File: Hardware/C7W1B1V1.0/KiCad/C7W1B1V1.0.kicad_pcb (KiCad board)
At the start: 2 copper layers, 20 x 20 mm, 0 parts

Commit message: początkowy schemat
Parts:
- added C1: 100n/16V/X5R, Capacitor_SMD:C_0402_1005Metric, F.Cu at (156.0, 74.0)
- added C10: 100n/16V/X5R, Capacitor_SMD:C_0402_1005Metric, F.Cu at (191.6, 52.9)
- added C11: 10u/6.3V/X5R, Capacitor_SMD:C_0402_1005Metric, F.Cu at (189.0, 69.0)
- added C12: 10u/6.3V/X5R, Capacitor_SMD:C_0402_1005Metric, F.Cu at (189.3, 73.0)
- added C13: 510p/10V/C0G, Capacitor_SMD:C_0402_1005Metric, F.Cu at (185.1, 75.7)
- added C14: 10u/6.3V/X5R, Capacitor_SMD:C_0402_1005Metric, F.Cu at (191.9, 69.0)
- added C15: 10u/6.3V/X5R, Capacitor_SMD:C_0402_1005Metric, F.Cu at (189.0, 71.0)
- added C16: 10u/6.3V/X5R, Capacitor_SMD:C_0402_1005Metric, F.Cu at (182.2, 77.7)
- added C17: 10u/6.3V/X5R, Capacitor_SMD:C_0402_1005Metric, F.Cu at (186.5, 73.0)
- added C18: 100n/16V/X5R, Capacitor_SMD:C_0402_1005Metric, F.Cu at (182.2, 75.7)
- added C19: 100n/16V/X5R, Capacitor_SMD:C_0402_1005Metric, F.Cu at (183.0, 86.0)
- added C2: 100n/16V/X5R, Capacitor_SMD:C_0402_1005Metric, F.Cu at (159.7, 69.2)
- added C20: 10u/6.3V/X5R, Capacitor_SMD:C_0402_1005Metric, F.Cu at (176.0, 92.5)
- added C21: 10u/6.3V/X5R, Capacitor_SMD:C_0402_1005Metric, F.Cu at (174.8, 97.0)
- added C22: 10u/6.3V/X5R, Capacitor_SMD:C_0402_1005Metric, F.Cu at (176.0, 90.5)
- added C23: 100n/16V/X5R, Capacitor_SMD:C_0402_1005Metric, F.Cu at (174.8, 95.0)
- added C3: 100n/16V/X5R, Capacitor_SMD:C_0402_1005Metric, F.Cu at (158.9, 72.0)
- added C4: 100n/16V/X5R, Capacitor_SMD:C_0402_1005Metric, F.Cu at (151.6, 76.4)
- added C5: 8p/16V/C0G, Capacitor_SMD:C_0402_1005Metric, F.Cu at (154.5, 76.4)
- added C6: 8p/16V/C0G, Capacitor_SMD:C_0402_1005Metric, F.Cu at (162.5, 69.2)
- added C7: 100n/16V/X5R, Capacitor_SMD:C_0402_1005Metric, F.Cu at (158.8, 52.9)
- added C8: 100n/16V/X5R, Capacitor_SMD:C_0402_1005Metric, F.Cu at (185.4, 61.0)
- added C9: 100n/16V/X5R, Capacitor_SMD:C_0402_1005Metric, F.Cu at (182.5, 63.0)
- added D1: PMEG4010CEGWX, Diode_SMD:D_SOD-123, F.Cu at (176.5, 69.7)
- added D2: BZX384B3V3-E3-08, Diode_SMD:D_SOD-323, F.Cu at (175.7, 77.0)
- added F1: 0686F2000-01, Fuse:Fuse_0603_1608Metric, F.Cu at (176.6, 86.3)
- added IC1: USBLC6-2P6, Footprints:USBLC62P6, F.Cu at (150.8, 97.9)
- added IC2: LMR62421XSD_NOPB, Footprints:SON95P300X300X80-7N, F.Cu at (182.0, 70.4)
- added IC3: S-8261AAXMD-G2XT2U, Footprints:SOT95P275X135-6N, F.Cu at (165.6, 96.4)
- added J1: Waveshare 12955, Connector_PinHeader_2.54mm:PinHeader_2x04_P2.54mm_Vertical, F.Cu at (149.6, 54.2)
- added J2: PMS3003, Connector_PinHeader_2.54mm:PinHeader_2x04_P2.54mm_Vertical, F.Cu at (176.2, 54.2)
- added J3: USB4105GFA120, Footprints:GCT_USB4105GFA120, F.Cu at (154.1, 91.7)
- added J4: Conn_01x02_Male, TerminalBlock:TerminalBlock_bornier-2_P5.08mm, F.Cu at (166.2, 89.5)
- added L1: CBC3225T470MR, Inductor_SMD:L_1210_3225Metric, F.Cu at (176.4, 73.5)
- added Q1: PMDPB30XNAX, Footprints:PMDPB30XNAX, F.Cu at (170.8, 96.6)
- added R1: 10k/5%/0.063W, Resistor_SMD:R_0402_1005Metric, F.Cu at (156.0, 72.0)
- added R10: 30k/1%/0.063W, Resistor_SMD:R_0402_1005Metric, F.Cu at (179.3, 76.6)
- added R11: 10k/1%/0.063W, Resistor_SMD:R_0402_1005Metric, F.Cu at (183.6, 73.7)
- added R12: 10k/1%/0.063W, Resistor_SMD:R_0402_1005Metric, F.Cu at (186.1, 71.0)
- added R13: 10k/1%/0.063W, Resistor_SMD:R_0402_1005Metric, F.Cu at (180.7, 73.7)
- added R14: 10k/5%/0.063W, Resistor_SMD:R_0402_1005Metric, F.Cu at (154.6, 100.5)
- added R15: 10k/5%/0.063W, Resistor_SMD:R_0402_1005Metric, F.Cu at (159.8, 96.1)
- added R16: 10k/5%/0.063W, Resistor_SMD:R_0402_1005Metric, F.Cu at (159.8, 99.7)
- added R17: 2k2/5%/0.063W, Resistor_SMD:R_0402_1005Metric, F.Cu at (162.7, 100.2)
- added R18: 2k2/5%/0.063W, Resistor_SMD:R_0402_1005Metric, F.Cu at (165.6, 99.7)
- added R19: 470/5%/0.063W, Resistor_SMD:R_0402_1005Metric, F.Cu at (176.0, 88.5)
- added R2: 10k/5%/0.063W, Resistor_SMD:R_0402_1005Metric, F.Cu at (148.7, 76.4)
- added R20: 100k/1%/0.063W, Resistor_SMD:R_0402_1005Metric, F.Cu at (159.0, 105.0)
- added R21: 100k/1%/0.063W, Resistor_SMD:R_0402_1005Metric, F.Cu at (161.9, 105.0)
- added R3: 10k/5%/0.063W, Resistor_SMD:R_0402_1005Metric, F.Cu at (155.9, 52.9)
- added R4: 10k/5%/0.063W, Resistor_SMD:R_0402_1005Metric, F.Cu at (182.6, 59.0)
- added R5: 10k/5%/0.063W, Resistor_SMD:R_0402_1005Metric, F.Cu at (188.7, 52.9)
- added R6: 10k/5%/0.063W, Resistor_SMD:R_0402_1005Metric, F.Cu at (182.6, 61.0)
- added R7: 10k/5%/0.063W, Resistor_SMD:R_0402_1005Metric, F.Cu at (185.5, 59.0)
- added R8: 10k/5%/0.063W, Resistor_SMD:R_0402_1005Metric, F.Cu at (188.7, 54.9)
- added R9: 10k/5%/0.063W, Resistor_SMD:R_0402_1005Metric, F.Cu at (186.1, 69.0)
- added U1: STM32L083CZTx, Package_QFP:LQFP-48_7x7mm_P0.5mm, F.Cu at (126.0, 71.0)
- added U2: BME688, Footprints:BME688, F.Cu at (184.2, 54.9)
- added U3: STC4054GR, Footprints:SOT95P280X110-5N, F.Cu at (155.8, 97.3)
- added Y1: 830106545501, Crystal:Crystal_SMD_2012-2Pin_2.0x1.2mm, F.Cu at (156.4, 69.6)

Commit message: Dodano projekt Cube
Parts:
- added C24: 100n/16V/X5R, Capacitor_SMD:C_0402_1005Metric, F.Cu at (86.6, 112.9)
- added C25: 100n/16V/X5R, Capacitor_SMD:C_0402_1005Metric, F.Cu at (83.7, 116.0)
- added C7: 100n/16V/X5R, Capacitor_SMD:C_0402_1005Metric, F.Cu at (-69.3, 121.4)
- added R22: 470/5%/0.063W, Resistor_SMD:R_0402_1005Metric, F.Cu at (92.7, 103.3)
- added R23: 100k/1%/0.063W, Resistor_SMD:R_0402_1005Metric, F.Cu at (83.5, 110.0)
- added R24: 100k/1%/0.063W, Resistor_SMD:R_0402_1005Metric, F.Cu at (89.8, 103.9)
- added U4: W25N512GVEIG, Footprints:SON127P800X600X80-9N-D, F.Cu at (-75.8, 142.7)
- added U5: STC4054GR, Footprints:SOT95P280X110-5N, F.Cu at (81.4, 104.7)
- C1, C2: value 100n/16V/X5R -> 8p/16V/C0G
- C11, C12: value 10u/6.3V/X5R -> 100n/16V/X5R
- C13: value 510p/10V/C0G -> 10u/6.3V/X5R
- C18: value 100n/16V/X5R -> 510p/10V/C0G
- C19, C23: value 100n/16V/X5R -> 10u/6.3V/X5R
- C21: value 10u/6.3V/X5R -> 10n/16V/X5R
- C5, C6: value 8p/16V/C0G -> 100n/16V/X5R
- J1: value Waveshare 12955 -> PMS3003
- J2: value PMS3003 -> USB4105GFA120; footprint Connector_PinHeader_2.54mm:PinHeader_2x04_P2.54mm_Vertical -> Footprints:GCT_USB4105GFA120
- J3: value USB4105GFA120 -> Conn_01x02_Male; footprint Footprints:GCT_USB4105GFA120 -> TerminalBlock:TerminalBlock_bornier-2_P5.08mm
- J4: value Conn_01x02_Male -> Waveshare 12955; footprint TerminalBlock:TerminalBlock_bornier-2_P5.08mm -> Connector_PinHeader_2.54mm:PinHeader_2x04_P2.54mm_Vertical
- R10: value 30k/1%/0.063W -> 10k/5%/0.063W
- R11, R12, R13: value 10k/1%/0.063W -> 10k/5%/0.063W
- R16: value 10k/5%/0.063W -> 2k2/5%/0.063W
- R17: value 2k2/5%/0.063W -> 30k/1%/0.063W
- R18: value 2k2/5%/0.063W -> 10k/1%/0.063W
- R19: value 470/5%/0.063W -> 2k2/5%/0.063W
- R20, R21: value 100k/1%/0.063W -> 10k/1%/0.063W
- U3: value STC4054GR -> MB85RS512TPNF-G-JNERE1; footprint Footprints:SOT95P280X110-5N -> Footprints:SOIC127P600X175-8N
- moved R8 281.2 mm to (-80.2, 137.2), turned to 270 degrees
- moved R5 271.9 mm to (-75.8, 116.0)
- moved C11 269.7 mm to (-73.0, 132.8)
- moved C12 268.7 mm to (-71.2, 138.8)
- moved R10 268.5 mm to (-80.9, 142.8), turned to 270 degrees
- moved C10 266.7 mm to (-63.6, 130.4), turned to 180 degrees
- moved R9 266.0 mm to (-71.6, 135.1), turned to 270 degrees
- moved U2 263.4 mm to (-72.8, 113.0), turned to 270 degrees
- moved C8 263.3 mm to (-73.3, 109.5), turned to 90 degrees
- moved R11 263.1 mm to (-70.6, 141.5), turned to 270 degrees
- moved R6 262.2 mm to (-73.8, 116.0)
- moved R7 261.0 mm to (-65.5, 130.4), turned to 180 degrees
- moved R4 260.7 mm to (-71.8, 116.0), turned to 180 degrees
- moved C26 259.7 mm to (-82.1, 149.9), turned to 270 degrees
- moved C9 258.7 mm to (-71.9, 109.9), turned to 180 degrees
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- renumbered C7 to C26
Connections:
- C1 pad 1: +3V3 -> GND
- C1 pad 2: GND -> Net-(C1-Pad2)
- C11 pad 1: +BATT -> +3V3
- C12 pad 1: +BATT -> +3V3
- C13 pad 1: +5V -> /Power/USB_VBUS
- C13 pad 2: Net-(C13-Pad2) -> GND
- C14 pad 1: +5V -> VBUS
- C14 pad 2: Net-(C14-Pad2) -> GND
- C15 pad 1: +5V -> +BATT
- C15 pad 2: Net-(C14-Pad2) -> GND
- C16 pad 1: +5V -> +BATT
- C16 pad 2: Net-(C14-Pad2) -> GND
- C17 pad 1: +5V -> VBUS
- C17 pad 2: Net-(C14-Pad2) -> GND
- C18 pad 2: Net-(C14-Pad2) -> Net-(C18-Pad2)
- C19 pad 1: +3V3 -> +5V
- C19 pad 2: GND -> Net-(C19-Pad2)
- C2 pad 1: +3V3 -> GND
- C2 pad 2: GND -> Net-(C2-Pad2)
- C20 pad 1: VBUS -> +5V
- C20 pad 2: GND -> Net-(C19-Pad2)
- C21 pad 1: VBUS -> 5V_TEST
- C22 pad 1: VBUS -> +5V
- C22 pad 2: GND -> Net-(C19-Pad2)
- C23 pad 1: +BATT -> +5V
- C23 pad 2: GND1 -> Net-(C19-Pad2)
- C5 pad 1: GND -> +3V3
- C5 pad 2: Net-(C5-Pad2) -> GND
- C6 pad 1: GND -> +3V3
- C6 pad 2: Net-(C6-Pad2) -> GND
- F1 pad 2: VBUS -> /Power/USB_VBUS
- IC2 pad 4: Net-(C13-Pad2) -> Net-(C18-Pad2)
- J1 pad 1: +3V3 -> +5V
- J1 pad 2: E_INC_BUSY -> PMS_SET
- J1 pad 3: E_INC_RST -> GND
- J1 pad 4: E_INC_DC -> PMS_RST
- J1 pad 5: GND -> Net-(J1-Pad5)
- J1 pad 6: SCK -> PMS_RX
- J1 pad 7: MOSI -> Net-(J1-Pad7)
- J1 pad 8: E_INC_CS -> PMS_TX
- J4 pad 1: GND1 -> +3V3
- J4 pad 2: +BATT -> GND
- R1 pad 1: +3V3 -> Net-(R1-Pad1)
- R1 pad 2: Net-(R1-Pad2) -> GND
- R10 pad 1: +5V -> +3V3
- R10 pad 2: Net-(C13-Pad2) -> Net-(R10-Pad2)
- R11 pad 1: Net-(C13-Pad2) -> +3V3
- R11 pad 2: GND -> Net-(R11-Pad2)
- R12 pad 1: +5V -> GND
- R12 pad 2: 5V_TEST -> Net-(J2-PadA5)
- R13 pad 1: 5V_TEST -> GND
- R13 pad 2: GND -> Net-(J2-PadB5)
- R14 pad 1: GND -> 5V_EN
- R14 pad 2: Net-(J3-PadA5) -> GND
- R15 pad 1: GND -> +3V3
- R15 pad 2: Net-(J3-PadB5) -> ~CHRG_STATUS
- R16 pad 1: +3V3 -> Net-(R16-Pad1)
- R16 pad 2: ~CHRG_STATUS -> GND
- R17 pad 1: Net-(R17-Pad1) -> +5V
- R17 pad 2: GND -> Net-(C18-Pad2)
- R18 pad 1: Net-(IC3-Pad2) -> Net-(C18-Pad2)
- R19 pad 1: Net-(IC3-Pad5) -> Net-(IC3-Pad2)
- R19 pad 2: +BATT -> GND
- R2 pad 1: Net-(R2-Pad1) -> +3V3
- R2 pad 2: GND -> Net-(R2-Pad2)
- R20 pad 1: +BATT -> +5V
- R20 pad 2: BATT -> 5V_TEST
- R21 pad 1: BATT -> 5V_TEST
- R3 pad 2: Net-(R3-Pad2) -> GND
- R4 pad 1: Net-(R4-Pad1) -> +3V3
- R4 pad 2: GND -> Net-(R4-Pad2)
- R5 pad 2: Net-(R5-Pad2) -> SDA
- R6 pad 2: SDA -> SCL
- R7 pad 1: +3V3 -> +5V
- R7 pad 2: SCL -> PMS_SET
- R8 pad 1: +5V -> +3V3
- R8 pad 2: Net-(J2-Pad2) -> Net-(R8-Pad2)
- R9 pad 1: 5V_EN -> +3V3
- R9 pad 2: GND -> Net-(R9-Pad2)
- U1 pad 13: Net-(U1-Pad13) -> ~FLASH_CS
- U1 pad 14: Net-(U1-Pad14) -> ~FRAM_CS
- U1 pad 17: Net-(U1-Pad17) -> MISO
- U1 pad 2: Net-(U1-Pad2) -> ~CHRG_STATUS
- U1 pad 21: Net-(U1-Pad21) -> E_INC_DC
- U1 pad 28: Net-(U1-Pad28) -> PMS_SET
- U1 pad 29: Net-(U1-Pad29) -> PMS_RST
- U1 pad 3: Net-(C5-Pad2) -> Net-(C1-Pad2)
- U1 pad 30: Net-(U1-Pad30) -> PMS_RX
- U1 pad 31: Net-(U1-Pad31) -> PMS_TX
- U1 pad 39: E_INC_DC -> Net-(U1-Pad39)
- U1 pad 4: Net-(C6-Pad2) -> Net-(C2-Pad2)
- U1 pad 44: Net-(R2-Pad1) -> Net-(R1-Pad1)
- U1 pad 7: Net-(R1-Pad2) -> Net-(R2-Pad2)
- U2 pad 2: Net-(R5-Pad2) -> Net-(R4-Pad2)
- U2 pad 5: Net-(R4-Pad1) -> Net-(R3-Pad1)
- U3 pad 1: ~CHRG_STATUS -> ~FRAM_CS
- U3 pad 2: GND -> MISO
- U3 pad 3: +BATT -> Net-(R8-Pad2)
- U3 pad 4: VBUS -> GND
- U3 pad 5: Net-(R17-Pad1) -> MOSI
- Y1 pad 1: Net-(C5-Pad2) -> Net-(C1-Pad2)
- Y1 pad 2: Net-(C6-Pad2) -> Net-(C2-Pad2)
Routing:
- net E_INC_DC: track 0.00 -> 40.8 mm
- net E_INC_CS: track 0.00 -> 32.9 mm
- net E_INC_BUSY: track 0.00 -> 32.7 mm
- net SCK: track 0.00 -> 28.8 mm
- net E_INC_RST: track 0.00 -> 28.7 mm
- net MOSI: track 0.00 -> 23.9 mm, vias 0 -> 2
- net MISO: track 0.00 -> 21.9 mm, vias 0 -> 2
- net ~FLASH_CS: track 0.00 -> 16.7 mm
- net +3V3: track 0.00 -> 14.2 mm, vias 0 -> 3
- net SDA: track 0.00 -> 8.64 mm
- net Net-(IC1-Pad3): track 0.00 -> 8.53 mm
- net Net-(IC1-Pad1): track 0.00 -> 7.60 mm
- net PMS_TX: track 0.00 -> 6.68 mm
- net ~FRAM_CS: track 0.00 -> 6.53 mm
- net /Power/USB_VBUS: track 0.00 -> 6.47 mm
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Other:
- board outline removed
- copper layers 2 -> 4
- net class Default: clearance 0.2 -> 0.16; trace_width 0.25 -> 0.16
- rule trace_clearance: 0.2 -> 0.16
- rule trace_min: 0.2 -> 0.16

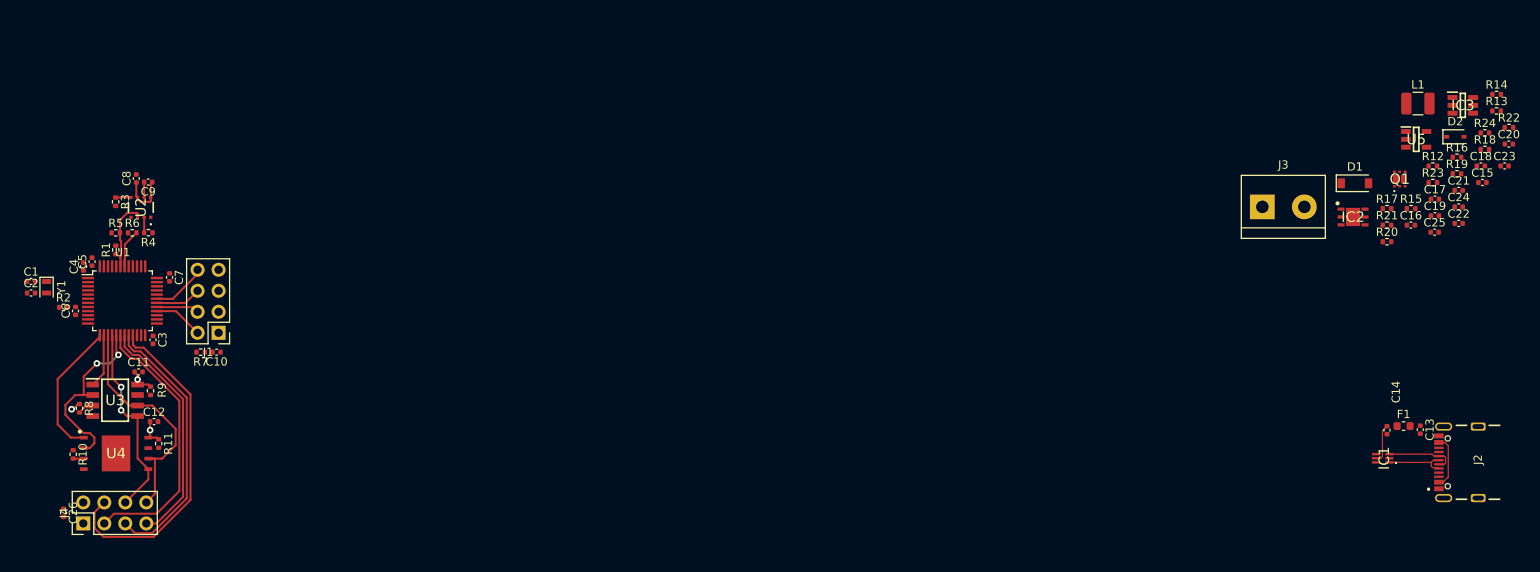
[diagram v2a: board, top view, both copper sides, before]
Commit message: Ukończono PCB. dodano pliki produkcyjne
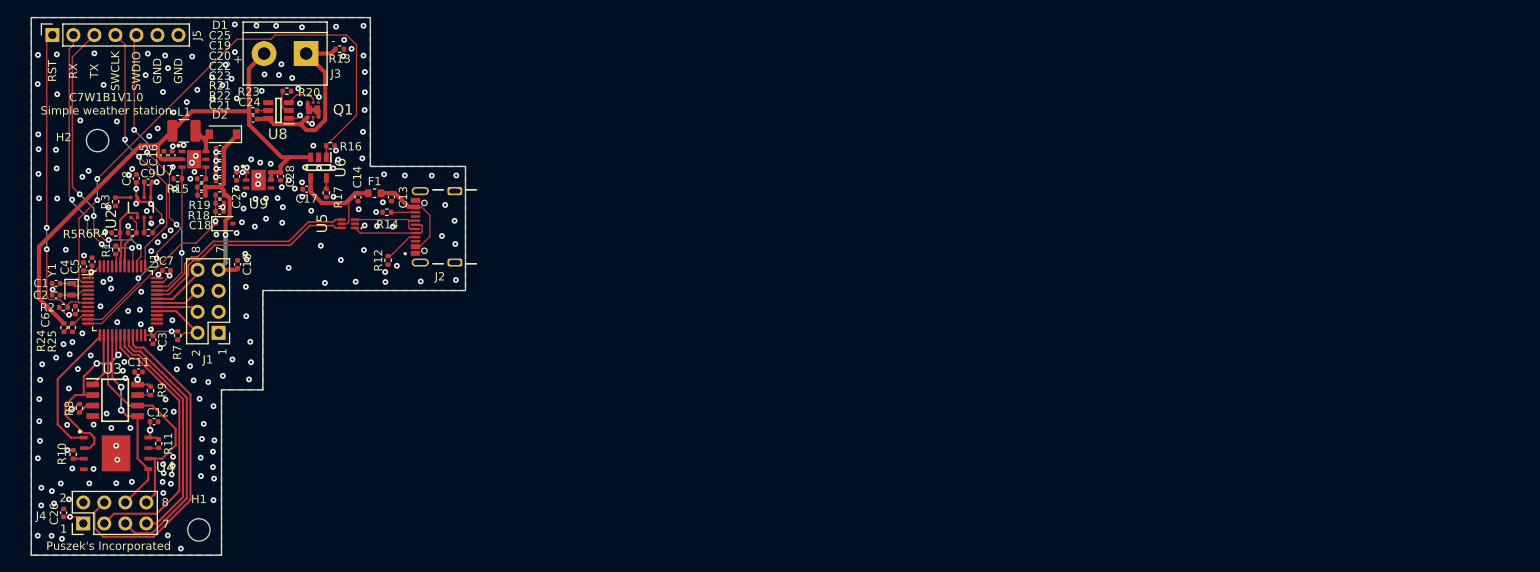
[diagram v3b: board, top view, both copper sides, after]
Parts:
- removed IC1: USBLC6-2P6, Footprints:USBLC62P6
- removed IC2: LMR62421XSD_NOPB, Footprints:SON95P300X300X80-7N
- removed IC3: S-8261AAXMD-G2XT2U, Footprints:SOT95P275X135-6N
- added C27: 10u/6.3V/X5R, Capacitor_SMD:C_0402_1005Metric, F.Cu at (-61.2, 109.2)
- added C28: 10u/6.3V/X5R, Capacitor_SMD:C_0402_1005Metric, F.Cu at (-55.9, 109.2)
- added H1: MountingHole, MountingHole:MountingHole_2.7mm_M2.5, F.Cu at (-65.7, 151.9)
- added H2: MountingHole, MountingHole:MountingHole_2.7mm_M2.5, F.Cu at (-78.0, 104.9)
- added J5: Conn_01x07, Connector_PinSocket_2.54mm:PinSocket_1x07_P2.54mm_Vertical, F.Cu at (-83.5, 92.1)
- added R25: 100k/1%/0.063W, Resistor_SMD:R_0402_1005Metric, F.Cu at (-81.0, 127.5)
- added U6: STC4054GR, Footprints:SOT95P280X110-5N, F.Cu at (-51.3, 108.1)
- added U7: LMR62421XSD_NOPB, Footprints:SON95P300X300X80-7N, F.Cu at (-66.3, 107.1)
- added U8: S-8261AAXMD-G2XT2U, Footprints:SOT95P275X135-6N, F.Cu at (-56.1, 101.2)
- added U9: LD39200PU33R, Footprints:SON95P300X300X100-7N-D, F.Cu at (-58.5, 109.7)
- R13: value 10k/5%/0.063W -> 0R
- R16: value 2k2/5%/0.063W -> 10k/5%/0.063W
- R17: value 30k/1%/0.063W -> 2k2/5%/0.063W
- R18: value 10k/1%/0.063W -> 30k/1%/0.063W
- R19: value 2k2/5%/0.063W -> 10k/1%/0.063W
- R20: value 10k/1%/0.063W -> 2k2/5%/0.063W
- R22: value 470/5%/0.063W -> 10k/1%/0.063W
- R23: value 100k/1%/0.063W -> 470/5%/0.063W
- U5: value STC4054GR -> USBLC6-2P6; footprint Footprints:SOT95P280X110-5N -> Footprints:USBLC62P6
- moved R24 173.4 mm to (-82.0, 127.5), turned to 270 degrees
- moved C15 159.4 mm to (-70.0, 106.6), turned to 90 degrees
- moved R22 156.1 mm to (-63.2, 112.4)
- moved C20 155.8 mm to (-63.2, 107.8), turned to 180 degrees
- moved C23 155.3 mm to (-63.2, 109.7), turned to 180 degrees
- moved R18 155.2 mm to (-65.4, 110.5), turned to 180 degrees
- moved C18 154.7 mm to (-65.4, 111.5), turned to 180 degrees
- moved R19 151.8 mm to (-65.4, 109.5), turned to 180 degrees
- moved C16 150.0 mm to (-69.0, 106.6), turned to 90 degrees
- moved C22 149.9 mm to (-63.2, 108.8), turned to 180 degrees
- moved C21 149.8 mm to (-63.2, 113.4)
- moved L1 149.2 mm to (-67.5, 103.7)
- moved D2 149.2 mm to (-62.7, 114.9)
- moved R15 149.2 mm to (-68.3, 109.5), turned to 180 degrees
- moved C25 147.2 mm to (-63.2, 105.8), turned to 180 degrees
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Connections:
- net Net-(R2-Pad2) renamed RST
- C19 pad 2: Net-(C19-Pad2) -> GND
- C20 pad 2: Net-(C19-Pad2) -> GND
- C22 pad 2: Net-(C19-Pad2) -> GND
- C23 pad 2: Net-(C19-Pad2) -> GND
- C25 pad 2: Net-(C19-Pad2) -> GND
- J1 pad 1: +5V -> Net-(J1-Pad1)
- J1 pad 7: Net-(J1-Pad7) -> +5V
- J2 pad A6: Net-(IC1-Pad3) -> Net-(J2-PadA6)
- J2 pad A7: Net-(IC1-Pad1) -> Net-(J2-PadA7)
- J2 pad B6: Net-(IC1-Pad3) -> Net-(J2-PadA6)
- J2 pad B7: Net-(IC1-Pad1) -> Net-(J2-PadA7)
- R13 pad 2: Net-(J2-PadB5) -> GND1
- R14 pad 1: 5V_EN -> GND
- R14 pad 2: GND -> Net-(J2-PadB5)
- R15 pad 1: +3V3 -> 5V_EN
- R15 pad 2: ~CHRG_STATUS -> GND
- R16 pad 1: Net-(R16-Pad1) -> +3V3
- R16 pad 2: GND -> ~CHRG_STATUS
- R17 pad 1: +5V -> Net-(R17-Pad1)
- R17 pad 2: Net-(C18-Pad2) -> GND
- R18 pad 1: Net-(C18-Pad2) -> +5V
- R18 pad 2: GND -> Net-(C18-Pad2)
- R19 pad 1: Net-(IC3-Pad2) -> Net-(C18-Pad2)
- R20 pad 1: +5V -> Net-(R20-Pad1)
- R20 pad 2: 5V_TEST -> GND
- R21 pad 1: 5V_TEST -> +5V
- R21 pad 2: GND -> 5V_TEST
- R22 pad 1: Net-(IC3-Pad5) -> 5V_TEST
- R22 pad 2: +BATT -> GND
- R23 pad 1: +BATT -> Net-(R23-Pad1)
- R23 pad 2: BATT -> +BATT
- R24 pad 1: BATT -> +BATT
- R24 pad 2: GND -> BATT
- R7 pad 1: +5V -> +3V3
- U1 pad 11: 5V_TEST -> 5V_EN
- U1 pad 12: 5V_EN -> 5V_TEST
- U1 pad 32: Net-(U1-Pad32) -> USB_D-
- U1 pad 33: Net-(U1-Pad33) -> USB_D+
- U1 pad 34: Net-(U1-Pad34) -> SWDIO
- U1 pad 37: Net-(U1-Pad37) -> SWCLK
- U1 pad 39: Net-(U1-Pad39) -> TX
- U1 pad 40: Net-(U1-Pad40) -> RX
- U5 pad 1: ~CHRG_STATUS -> Net-(J2-PadA7)
- U5 pad 3: +BATT -> Net-(J2-PadA6)
- U5 pad 4: VBUS -> USB_D+
- U5 pad 5: Net-(R16-Pad1) -> VBUS
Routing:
- net +BATT: track 0.00 -> 69.9 mm
- net ~CHRG_STATUS: track 0.00 -> 68.4 mm, vias 0 -> 2
- net RST: track 0.00 -> 38.0 mm, vias 0 -> 2
- net SWDIO: track 0.00 -> 34.9 mm, vias 0 -> 4
- net TX: track 0.00 -> 34.7 mm, vias 0 -> 4
- net RX: track 0.00 -> 33.3 mm, vias 0 -> 4
- net SWCLK: track 0.00 -> 31.6 mm, vias 0 -> 2
- net +3V3: track 14.2 -> 45.0 mm, vias 3 -> 21
- net USB_D-: track 0.00 -> 26.6 mm
- net USB_D+: track 0.00 -> 26.6 mm
- net 5V_EN: track 0.00 -> 24.1 mm, vias 0 -> 2
- net 5V_TEST: track 0.00 -> 23.9 mm, vias 0 -> 1
- net +5V: track 0.00 -> 23.5 mm, vias 0 -> 1
- net GND1: track 0.00 -> 23.5 mm
- net Net-(J2-PadA7): track 0.00 -> 10.0 mm
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- added copper zone on In1.Cu, net +3V3
- added copper zone on B.Cu, net GND
- added copper zone on F.Cu, net GND
- added copper zone on In2.Cu, net GND
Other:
- board outline added: 52.5 x 65 mm
- net class Default: via_dia 0.8 -> 0.7; via_drill 0.4 -> 0.3
- net class Power added: clearance 0.16, trace_width 0.5, via_dia 0.7, via_drill 0.3
- board text added: "+"
- board text added: "-"
- board text added: "1"
- board text added: "2"
- board text added: "7"
- board text added: "8"
- board text added: "C7W1B1V1.0 Simple weather station"
- board text added: "GND"
- board text added: "Puszek's Incorporated"
- board text added: "RST"
- board text added: "RX"
- board text added: "SWCLK"
- board text added: "SWDIO"
- board text added: "TX"

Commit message: Zmieniono procesor na wersję LQFP-64
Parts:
- added C29: 100n/16V/X5R, Capacitor_SMD:C_0402_1005Metric, F.Cu at (-77.1, 131.6)
- R23: value 470/5%/0.063W -> 470R/5%/0.063W
- U1: value STM32L083CZTx -> STM32L083RZTx; footprint Package_QFP:LQFP-48_7x7mm_P0.5mm -> Package_QFP:LQFP-64_10x10mm_P0.5mm
- moved R7 3.85 mm to (-65.2, 126.2), turned to 90 degrees
- moved C10 3.55 mm to (-57.6, 120.5)
- moved J1 3.37 mm to (-60.0, 128.3)
- moved C3 2.83 mm to (-70.0, 131.5), turned to 180 degrees
- moved C7 2.44 mm to (-67.4, 119.6)
- moved R2 1.63 mm to (-81.4, 123.6)
- moved C5 1.48 mm to (-78.3, 118.1)
- moved C4 1.48 mm to (-79.4, 118.7)
- moved U1 1.31 mm to (-73.7, 124.3)
- moved C1 1.16 mm to (-83.3, 121.0)
- moved C2 1.16 mm to (-83.3, 122.4)
- moved Y1 1.16 mm to (-81.4, 121.7)
- moved R1 1.10 mm to (-76.1, 117.0), turned to 180 degrees
- moved C6 0.37 mm to (-80.9, 125.6)
- moved C11 0.19 mm to (-73.2, 132.8)
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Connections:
- U1 pad 10: BATT -> Net-(U1-Pad10)
- U1 pad 11: 5V_EN -> Net-(U1-Pad11)
- U1 pad 12: 5V_TEST -> GND
- U1 pad 13: ~FLASH_CS -> +3V3
- U1 pad 14: ~FRAM_CS -> BATT
- U1 pad 15: SCK -> 5V_EN
- U1 pad 16: MOSI -> 5V_TEST
- U1 pad 17: MISO -> ~FLASH_CS
- U1 pad 18: E_INC_CS -> GND
- U1 pad 19: E_INC_RST -> +3V3
- U1 pad 20: E_INC_BUSY -> ~FRAM_CS
- U1 pad 21: E_INC_DC -> SCK
- U1 pad 22: Net-(U1-Pad22) -> MISO
- U1 pad 23: GND -> MOSI
- U1 pad 24: +3V3 -> E_INC_CS
- U1 pad 25: Net-(U1-Pad25) -> E_INC_RST
- U1 pad 26: Net-(U1-Pad26) -> E_INC_BUSY
- U1 pad 27: Net-(U1-Pad27) -> E_INC_DC
- U1 pad 28: PMS_SET -> Net-(U1-Pad28)
- U1 pad 29: PMS_RST -> Net-(U1-Pad29)
- U1 pad 30: PMS_RX -> Net-(U1-Pad30)
- U1 pad 31: PMS_TX -> GND
- U1 pad 32: USB_D- -> +3V3
- U1 pad 33: USB_D+ -> Net-(U1-Pad33)
- U1 pad 34: SWDIO -> Net-(U1-Pad34)
- U1 pad 35: GND -> Net-(U1-Pad35)
- U1 pad 36: +3V3 -> Net-(U1-Pad36)
- U1 pad 37: SWCLK -> Net-(U1-Pad37)
- U1 pad 39: TX -> Net-(U1-Pad39)
- U1 pad 40: RX -> PMS_SET
- U1 pad 41: Net-(U1-Pad41) -> PMS_RST
- U1 pad 42: SCL -> PMS_RX
- U1 pad 43: SDA -> PMS_TX
- U1 pad 44: Net-(R1-Pad1) -> USB_D-
- U1 pad 45: Net-(U1-Pad45) -> USB_D+
- U1 pad 46: Net-(U1-Pad46) -> SWDIO
- U1 pad 8: GND -> Net-(U1-Pad8)
- U1 pad 9: +3V3 -> Net-(U1-Pad9)
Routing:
- net SCK: track 28.8 -> 24.3 mm
- net E_INC_DC: track 40.8 -> 36.6 mm
- net E_INC_RST: track 28.7 -> 24.7 mm
- net USB_D+: track 26.6 -> 22.7 mm
- net USB_D-: track 26.6 -> 22.7 mm
- net E_INC_CS: track 32.9 -> 29.2 mm
- net E_INC_BUSY: track 32.7 -> 29.1 mm
- net ~FLASH_CS: track 16.7 -> 13.7 mm, vias 0 -> 2
- net GND: track 4.38 -> 7.04 mm, vias 225 -> 234
- net MOSI: track 23.9 -> 21.4 mm
- net SWCLK: track 31.6 -> 29.2 mm
- net PMS_SET: track 8.95 -> 7.01 mm
- net 5V_TEST: track 23.9 -> 25.8 mm, vias 1 -> 0
- net SDA: track 8.64 -> 6.81 mm
- net SCL: track 6.80 -> 5.31 mm
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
